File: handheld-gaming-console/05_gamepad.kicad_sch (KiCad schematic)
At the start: 19 parts, among them SW3 RESET, SW4 BOOTSEL, U11 RP2040, U12 W25Q32JVSS, Y2 12MHz

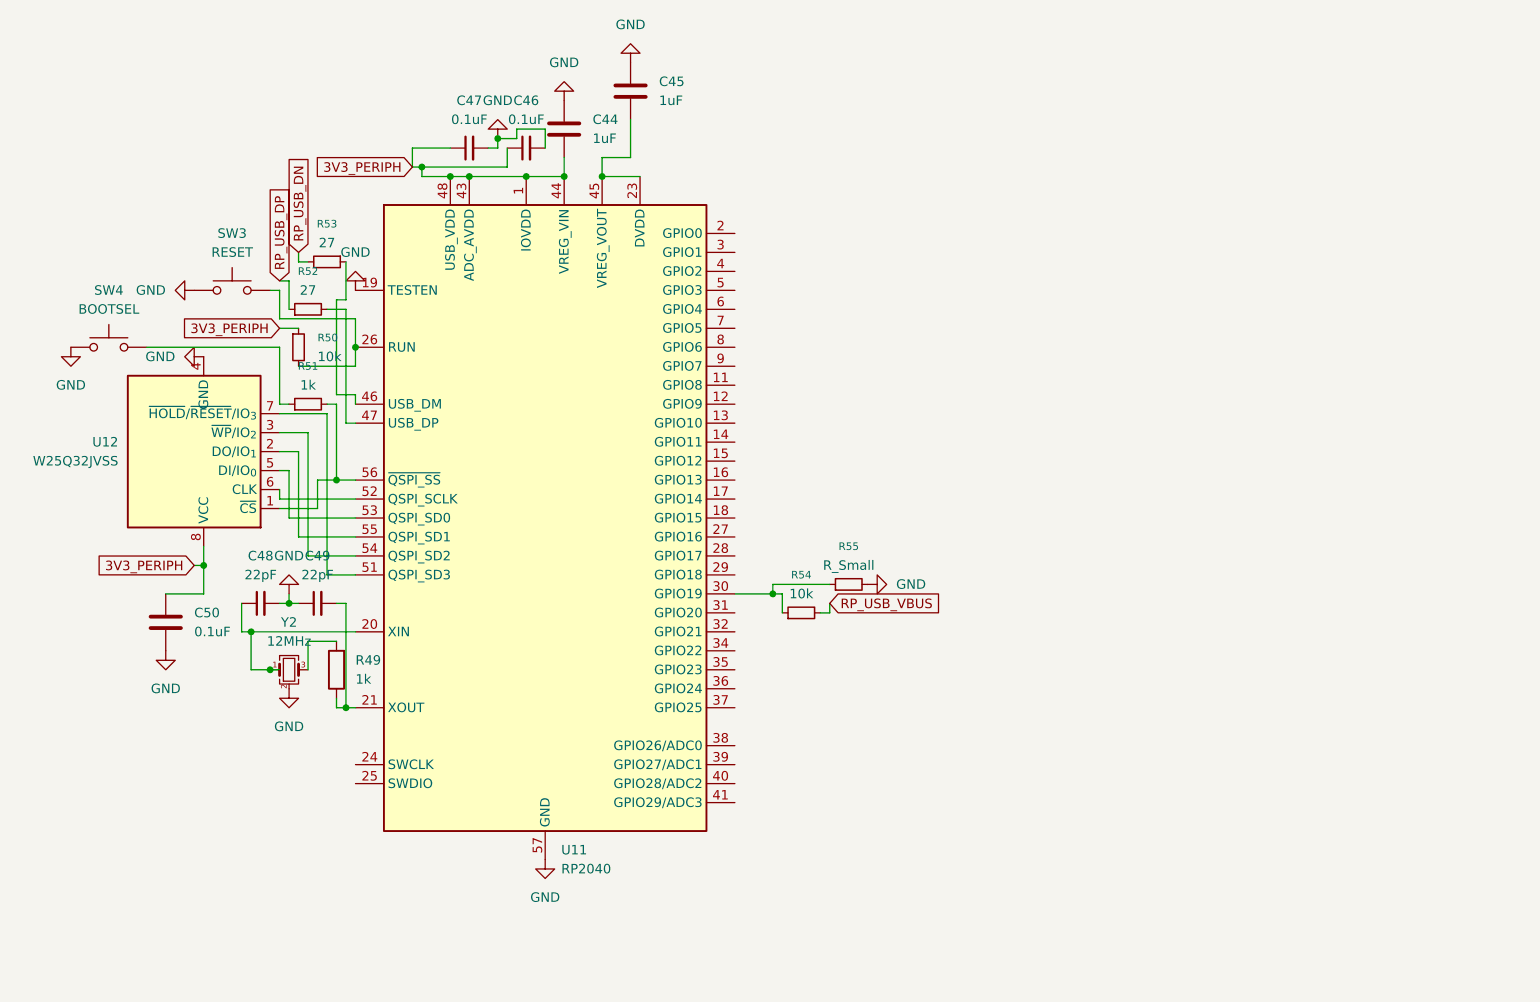
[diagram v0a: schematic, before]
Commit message: feat(gamepad): wire dual analog thumbstick RC filters and map 16 direct-GPIO hardware buttons
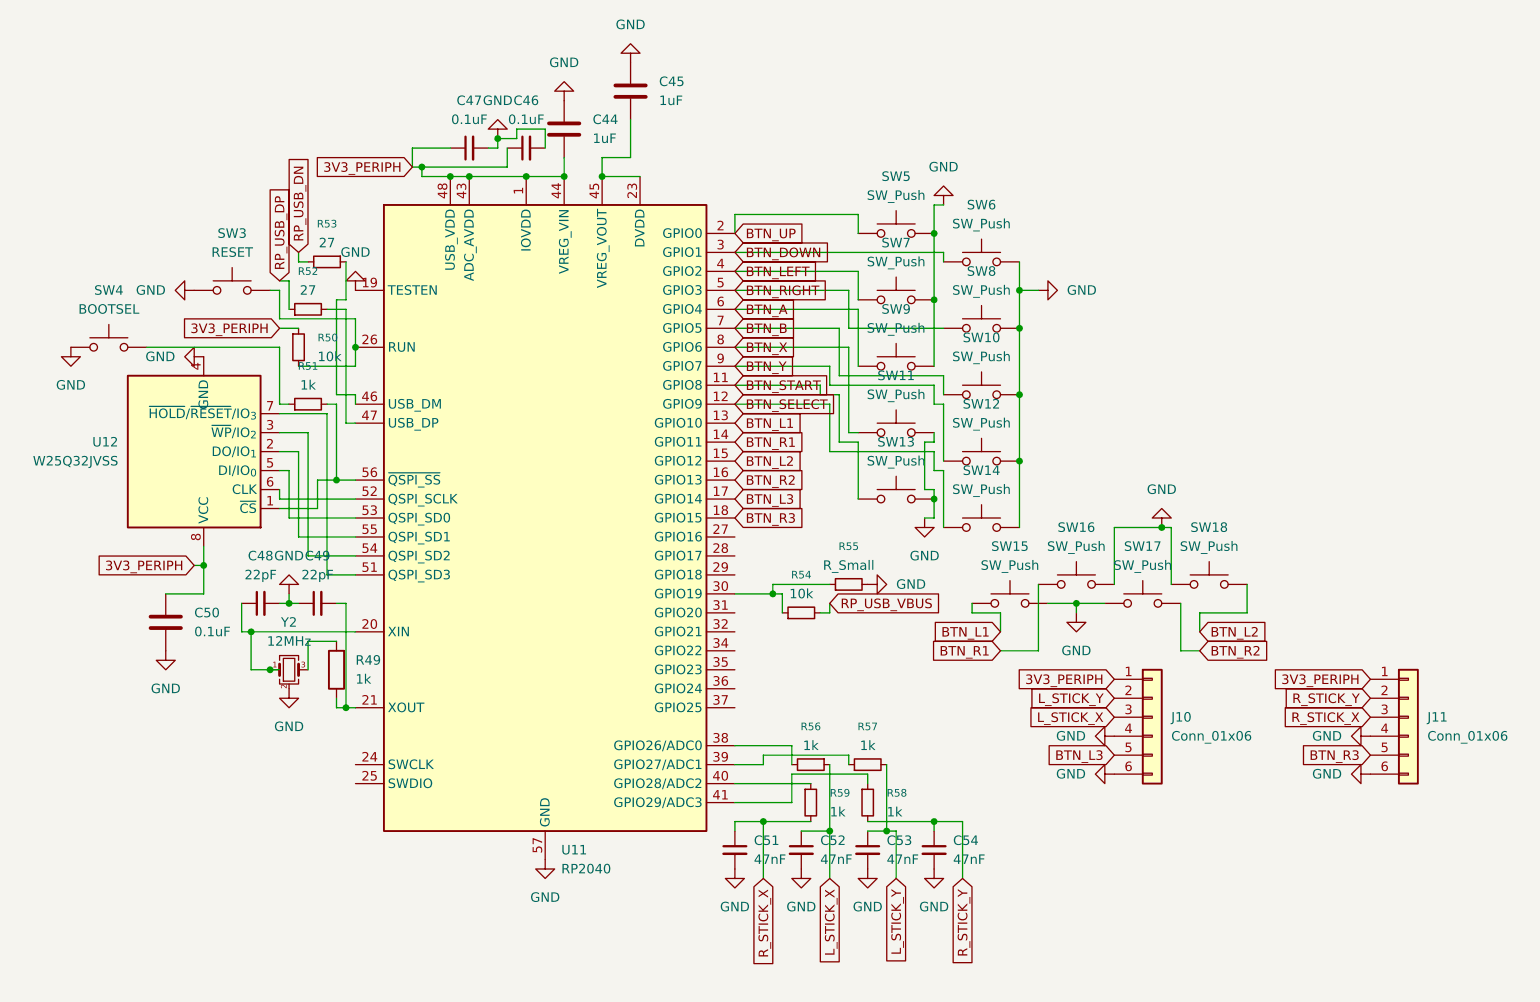
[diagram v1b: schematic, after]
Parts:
- added C51, C52, C53, C54: 47nF, symbol Device:C_Small
- added J10, J11: Conn_01x06, symbol Connector_Generic:Conn_01x06
- added R56, R57, R58, R59: 1k, symbol Device:R_Small
- added SW10, SW11, SW12, SW13, SW14, SW15, SW16, SW17, SW18, SW5, SW6, SW7, SW8, SW9: SW_Push, symbol Switch:SW_Push
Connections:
- net 3V3_PERIPH: now also J10.1 (Pin_1), J11.1 (Pin_1)
- net GND: now also C51.2, C52.2, C53.2, C54.2, J10.4 (Pin_4), J10.6 (Pin_6), J11.4 (Pin_4), J11.6 (Pin_6), SW10.2, SW11.2, SW12.2, SW13.2, SW14.2, SW15.2, SW16.2, SW17.1, SW18.1, SW5.2, SW6.2, SW7.2, SW8.2, SW9.2
- net BTN_START: now reaches U11.11 (GPIO8)
- net BTN_START: now also SW13.1
- net BTN_SELECT: now reaches U11.12 (GPIO9)
- net BTN_SELECT: now also SW14.1
- net BTN_L1: now reaches U11.13 (GPIO10)
- net BTN_L1: now also SW15.1
- net BTN_R1: now reaches U11.14 (GPIO11)
- net BTN_R1: now also SW16.1
- net BTN_L2: now reaches U11.15 (GPIO12)
- net BTN_L2: now also SW18.2
- net BTN_R2: now reaches U11.16 (GPIO13)
- net BTN_R2: now also SW17.2
- net BTN_L3: now reaches U11.17 (GPIO14)
- net BTN_L3: now also J10.5 (Pin_5)
- net BTN_R3: now reaches U11.18 (GPIO15)
- net BTN_R3: now also J11.5 (Pin_5)
- net BTN_UP: now reaches U11.2 (GPIO0)
- net BTN_UP: now also SW5.1
- net BTN_DOWN: now reaches U11.3 (GPIO1)
- net BTN_DOWN: now also SW6.1
- net at U11.38 (GPIO26/ADC0): now also R56.2
- net at U11.39 (GPIO27/ADC1): now also R57.1
- net BTN_LEFT: now reaches U11.4 (GPIO2)
- net BTN_LEFT: now also SW7.1
- net at U11.40 (GPIO28/ADC2): now also R59.1
- net at U11.41 (GPIO29/ADC3): now also R58.1
- net BTN_RIGHT: now reaches U11.5 (GPIO3)
- net BTN_RIGHT: now also SW8.1
- net BTN_A: now reaches U11.6 (GPIO4)
- net BTN_A: now also SW9.1
- net BTN_B: now reaches U11.7 (GPIO5)
- net BTN_B: now also SW10.1
- net BTN_X: now reaches U11.8 (GPIO6)
- net BTN_X: now also SW11.1
- net BTN_Y: now reaches U11.9 (GPIO7)
- net BTN_Y: now also SW12.1
- new net L_STICK_X: C52.1, J10.3 (Pin_3), R56.1
- new net L_STICK_Y: C53.1, J10.2 (Pin_2), R57.2
- new net R_STICK_X: C51.1, J11.3 (Pin_3), R59.2
- new net R_STICK_Y: C54.1, J11.2 (Pin_2), R58.2
